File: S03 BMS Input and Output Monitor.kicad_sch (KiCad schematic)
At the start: 29 parts, among them Q4 DMP3007SCG-13, Q5 DMP3007SCG-13, U1 LTC1960

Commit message: Keep top copper out of power FET source-drain gaps; mask-layer logo
- Add F.Cu keepouts (no tracks/vias/pour) between source and drain pads
  in the TDSON, CSD17304Q3 and PowerDI3333 footprints, so a shorted FET
  can be reworked without bridging S-D through top copper.
- Add Diodes_PowerDI3333-8 (copy of the KiCad Package_SON footprint with
  the keepout) and point Q4/Q5/Q12-Q15 at it; drop the board-level
  Q5/Q7 keepouts.
- Move nine vias (Q17 GND, Q18 SW2) out of the S-D gaps.
- New dru rule "Power FET pad to pour": 0.3 mm zone-to-pad clearance on
  Q footprints, giving >=0.25 mm mask web around FET pads.
- Add EVOSONIC_DNA_LOGO_390X600_MASK footprint (F.Mask polygons) and
  use it for LOGO01.
- Schematic NOTE fields updated and pushed to the PCB; zones refilled.
- README notes on the keepouts and the 0.3 mm rule.

ERC 0 violations. DRC 0 unconnected, 0 parity; remaining items are
excluded layer-marker edge clearances, silk overlap and text thickness.

Co-Authored-By: Claude Opus 5.5 <noreply@anthropic.com>
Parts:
- Q4, Q5: footprint Package_SON:Diodes_PowerDI3333-8 -> EVO2513-0_5_0-import-fps:Diodes_PowerDI3333-8
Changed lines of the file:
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@@
 			)
 		)
-		(property "Footprint" "Package_SON:Diodes_PowerDI3333-8"
+		(property "Footprint" "EVO2513-0_5_0-import-fps:Diodes_PowerDI3333-8"
 			(at 260.35 83.82 0)
 			(hide yes)
@@
 			)
 		)
-		(property "Footprint" "Package_SON:Diodes_PowerDI3333-8"
+		(property "Footprint" "EVO2513-0_5_0-import-fps:Diodes_PowerDI3333-8"
 			(at 275.59 83.82 0)
 			(hide yes)

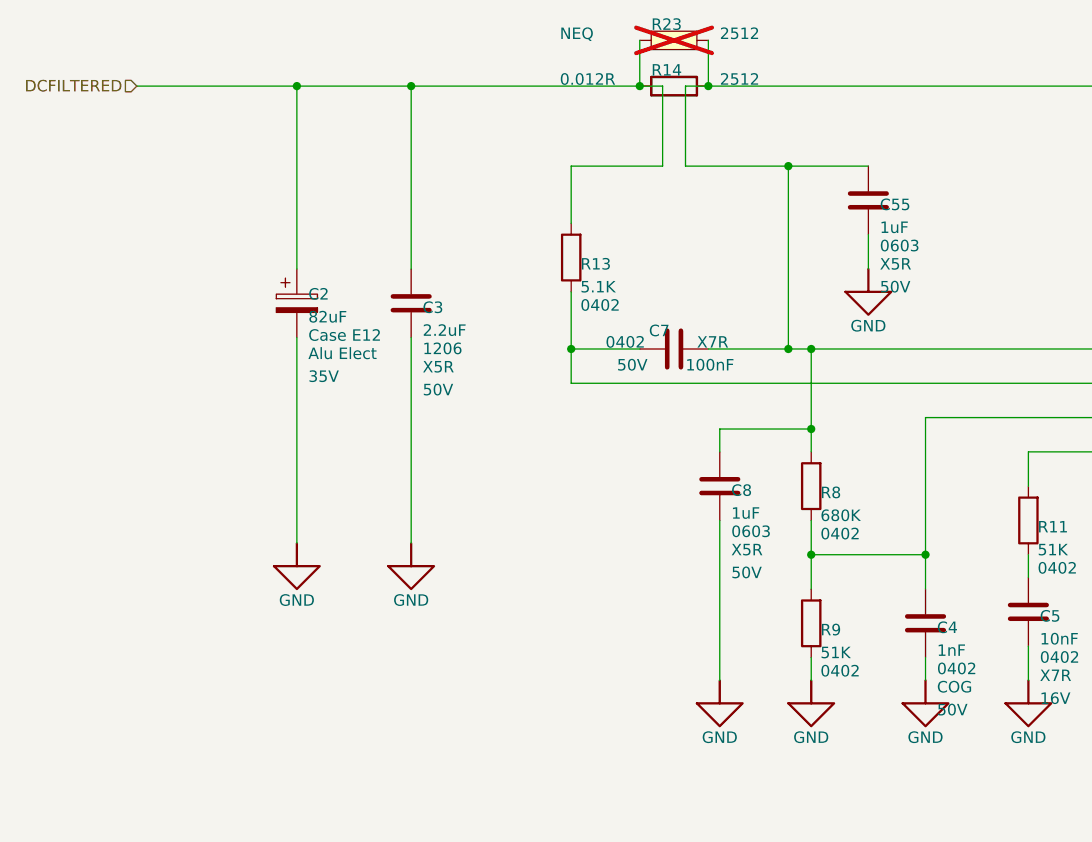
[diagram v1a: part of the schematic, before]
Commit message: Remove C55; charger layout; QC and S/N boxes
- C55 removed from the schematic and board.
- Charger-area placement and routing around U1 (C8, C7, R13, D3, DCSENSED).
- Filled QC and S/N marking boxes on the front silkscreen.

DRC: 23 violations (silk/text only), 0 unconnected, 0 parity.

Co-Authored-By: Claude Opus 5.5 <noreply@anthropic.com>
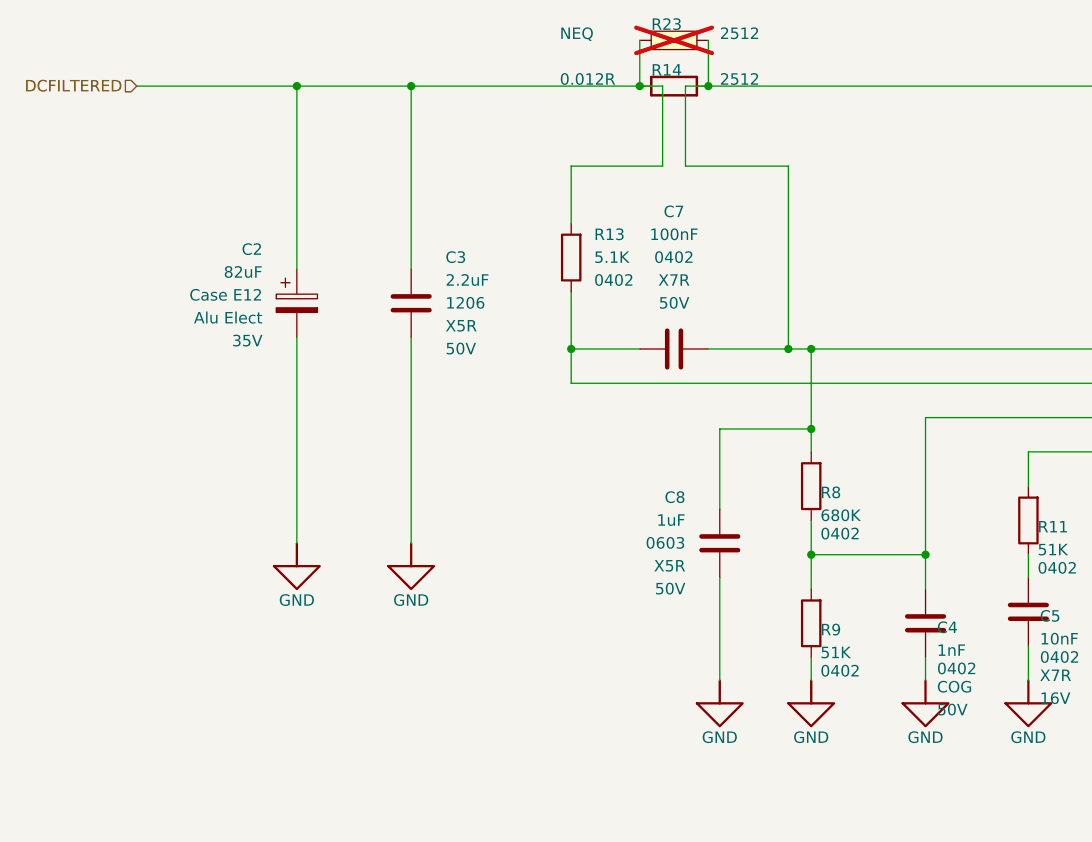
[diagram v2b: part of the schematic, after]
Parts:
- removed C55: 1uF, Capacitor_SMD:C_0603_1608Metric, symbol Device:C
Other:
- moved on the sheet: C8

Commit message: Fill manufacturer part numbers from the 0.5.0 build orders
Set MANUFACTURER and MANUFACTURER_PN on every fitted part, in the
schematic and on the board. Unchanged parts take the exact part numbers
ordered for the 0.5.0 backup build (DigiKey list and Mouser basket);
changed parts reuse an ordered part where value, package and rating
match; the rest keep the schematic's part or take a Yageo RC/CC part.

Co-Authored-By: Claude Opus 5.5 <noreply@anthropic.com>
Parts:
- C10, C7, R14: MANUFACTURER Yageo -> YAGEO
- C11, C12: MANUFACTURER Murata -> Murata Electronics
- C2: MANUFACTURER Panasonic -> Panasonic Industry
- C3: MANUFACTURER (none) -> YAGEO; MANUFACTURER_PN (none) -> CC1206KKX5R9BB225
- C4: MANUFACTURER (none) -> YAGEO; MANUFACTURER_PN (none) -> AC0402JRNPO9BN102
- C5: MANUFACTURER Murata -> Murata Electronics; MANUFACTURER_PN GRM155R71C103K -> GRM155R71C103KA01D
- C57: MANUFACTURER ? -> YAGEO; MANUFACTURER_PN ? -> CC0402JRNPO9BN101
- C6: MANUFACTURER (none) -> KEMET; MANUFACTURER_PN (none) -> C0402C182K4RACTU
- C8, C9: MANUFACTURER ? -> Samsung Electro-Mechanics; MANUFACTURER_PN ? -> CL10A105KB8NNNC
- R10: MANUFACTURER ? -> YAGEO; MANUFACTURER_PN ? -> RC0402FR-074K7L
- R11, R9: MANUFACTURER (none) -> YAGEO; MANUFACTURER_PN (none) -> RC0402FR-0751KL
- R12, R18: MANUFACTURER ? -> YAGEO; MANUFACTURER_PN ? -> RC0402FR-07100KL
- R13: MANUFACTURER ? -> YAGEO; MANUFACTURER_PN ? -> RC0402FR-075K1L
- R15: MANUFACTURER ? -> YAGEO; MANUFACTURER_PN ? -> RC0402FR-07100RL
- R16: MANUFACTURER Bourns -> Bourns Inc.
- R17: MANUFACTURER ? -> YAGEO; MANUFACTURER_PN ? -> RC0402FR-07619KL
- R8: MANUFACTURER (none) -> YAGEO; MANUFACTURER_PN (none) -> RC0402FR-07680KL
- U1: MANUFACTURER Analog Devices -> Analog Devices Inc.; MANUFACTURER_PN LTC1960CUHF -> LTC1960CUHF#PBF
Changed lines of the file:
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@@
 			)
 		)
-		(property "MANUFACTURER" "?"
+		(property "MANUFACTURER" "YAGEO"
 			(at 128.524 193.802 0)
 			(hide yes)
@@
 			)
 		)
-		(property "MANUFACTURER_PN" "?"
+		(property "MANUFACTURER_PN" "RC0402FR-07100KL"
 			(at 128.524 193.802 0)
 			(hide yes)
@@
 			)
 		)
-		(property "MANUFACTURER" "Analog Devices"
+		(property "MANUFACTURER" "Analog Devices Inc."
 			(at 193.802 130.81 0)
 			(hide yes)
@@
 			)
 		)
-		(property "MANUFACTURER_PN" "LTC1960CUHF"
+		(property "MANUFACTURER_PN" "LTC1960CUHF#PBF"
 			(at 193.802 130.81 0)
 			(hide yes)
@@
 			)
 		)
-		(property "MANUFACTURER" "?"
+		(property "MANUFACTURER" "Samsung Electro-Mechanics"
 			(at 220.98 137.922 0)
 			(hide yes)
@@
 			)
 		)
-		(property "MANUFACTURER_PN" "?"
+		(property "MANUFACTURER_PN" "CL10A105KB8NNNC"
 			(at 220.98 137.922 0)
 			(hide yes)
@@
 			)
 		)
-		(property "MANUFACTURER" "?"
+		(property "MANUFACTURER" "YAGEO"
 			(at 221.234 129.032 0)
 			(hide yes)
@@
 			)
 		)
-		(property "MANUFACTURER_PN" "?"
+		(property "MANUFACTURER_PN" "RC0402FR-07100RL"
 			(at 221.234 129.032 0)
 			(hide yes)
@@
 			)
 		)
-		(property "MANUFACTURER" ""
+		(property "MANUFACTURER" "YAGEO"
 			(at 85.09 103.632 0)
 			(hide yes)
@@
 			)
 		)
-		(property "MANUFACTURER_PN" ""
+		(property "MANUFACTURER_PN" "CC1206KKX5R9BB225"
 			(at 85.09 103.632 0)
 			(hide yes)
@@
 			)
 		)
-		(property "MANUFACTURER" "?"
+		(property "MANUFACTURER" "YAGEO"
 			(at 112.014 193.802 0)
 			(hide yes)
@@
 			)
 		)
-		(property "MANUFACTURER_PN" "?"
+		(property "MANUFACTURER_PN" "RC0402FR-074K7L"
 			(at 112.014 193.802 0)
 			(hide yes)
@@
 			)
 		)
-		(property "MANUFACTURER" "Yageo"
+		(property "MANUFACTURER" "YAGEO"
 			(at 111.252 111.76 90)
 			(hide yes)
@@
 			)
 		)
-		(property "MANUFACTURER" ""
+		(property "MANUFACTURER" "KEMET"
 			(at 162.052 138.43 0)
 			(hide yes)
@@
 			)
 		)
-		(property "MANUFACTURER_PN" ""
+		(property "MANUFACTURER_PN" "C0402C182K4RACTU"
 			(at 162.052 138.43 0)
 			(hide yes)
@@
 			)
 		)
-		(property "MANUFACTURER" "Panasonic"
+		(property "MANUFACTURER" "Panasonic Industry"
 			(at 72.39 103.632 0)
 			(hide yes)
@@
 			)
 		)
-		(property "MANUFACTURER" "Yageo"
+		(property "MANUFACTURER" "YAGEO"
 			(at 234.95 130.302 0)
 			(hide yes)
@@
 			)
 		)
-		(property "MANUFACTURER" "Analog Devices"
+		(property "MANUFACTURER" "Analog Devices Inc."
 			(at 164.592 224.79 0)
 			(hide yes)
@@
 			)
 		)
-		(property "MANUFACTURER_PN" "LTC1960CUHF"
+		(property "MANUFACTURER_PN" "LTC1960CUHF#PBF"
 			(at 164.592 224.79 0)
 			(hide yes)
@@
 			)
 		)
-		(property "MANUFACTURER" "Murata"
+		(property "MANUFACTURER" "Murata Electronics"
 			(at 256.54 181.102 0)
 			(hide yes)
@@
 			)
 		)
-		(property "MANUFACTURER" ""
+		(property "MANUFACTURER" "YAGEO"
 			(at 129.794 123.952 0)
 			(hide yes)
@@
 			)
 		)
-		(property "MANUFACTURER_PN" ""
+		(property "MANUFACTURER_PN" "RC0402FR-07680KL"
 			(at 129.794 123.952 0)
 			(hide yes)
@@
 			)
 		)
-		(property "MANUFACTURER" "?"
+		(property "MANUFACTURER" "YAGEO"
 			(at 254 220.472 0)
 			(hide yes)
@@
 			)
 		)
-		(property "MANUFACTURER_PN" "?"
+		(property "MANUFACTURER_PN" "CC0402JRNPO9BN101"
 			(at 254 220.472 0)
 			(hide yes)
@@
 			)
 		)
-		(property "MANUFACTURER" "?"
+		(property "MANUFACTURER" "Samsung Electro-Mechanics"
 			(at 119.38 130.302 0)
 			(hide yes)
@@
 			)
 		)
-		(property "MANUFACTURER_PN" "?"
+		(property "MANUFACTURER_PN" "CL10A105KB8NNNC"
 			(at 119.38 130.302 0)
 			(hide yes)
@@
 			)
 		)
-		(property "MANUFACTURER" ""
+		(property "MANUFACTURER" "YAGEO"
 			(at 153.924 127.762 0)
 			(hide yes)
@@
 			)
 		)
-		(property "MANUFACTURER_PN" ""
+		(property "MANUFACTURER_PN" "RC0402FR-0751KL"
 			(at 153.924 127.762 0)
 			(hide yes)
@@
 			)
 		)
-		(property "MANUFACTURER" "?"
+		(property "MANUFACTURER" "YAGEO"
 			(at 240.284 220.472 0)
 			(hide yes)
@@
 			)
 		)
-		(property "MANUFACTURER_PN" "?"
+		(property "MANUFACTURER_PN" "RC0402FR-07100KL"
 			(at 240.284 220.472 0)
 			(hide yes)
@@
 			)
 		)
-		(property "MANUFACTURER" ""
+		(property "MANUFACTURER" "YAGEO"
 			(at 139.192 139.7 0)
 			(hide yes)
@@
 			)
 		)
-		(property "MANUFACTURER_PN" ""
+		(property "MANUFACTURER_PN" "AC0402JRNPO9BN102"
 			(at 139.192 139.7 0)
 			(hide yes)
@@
 			)
 		)
-		(property "MANUFACTURER" ""
+		(property "MANUFACTURER" "YAGEO"
 			(at 129.794 139.192 0)
 			(hide yes)
@@
 			)
 		)
-		(property "MANUFACTURER_PN" ""
+		(property "MANUFACTURER_PN" "RC0402FR-0751KL"
 			(at 129.794 139.192 0)
 			(hide yes)
@@
 			)
 		)
-		(property "MANUFACTURER" "Yageo"
+		(property "MANUFACTURER" "YAGEO"
 			(at 111.252 80.01 90)
 			(hide yes)
@@
 			)
 		)
-		(property "MANUFACTURER" "Murata"
+		(property "MANUFACTURER" "Murata Electronics"
 			(at 153.67 137.922 0)
 			(hide yes)
@@
 			)
 		)
-		(property "MANUFACTURER_PN" "GRM155R71C103K"
+		(property "MANUFACTURER_PN" "GRM155R71C103KA01D"
 			(at 153.67 137.922 0)
 			(hide yes)
@@
 			)
 		)
-		(property "MANUFACTURER" "Murata"
+		(property "MANUFACTURER" "Murata Electronics"
 			(at 269.24 181.102 0)
 			(hide yes)
@@
 			)
 		)
-		(property "MANUFACTURER" "?"
+		(property "MANUFACTURER" "YAGEO"
 			(at 103.124 98.552 0)
 			(hide yes)
@@
 			)
 		)
-		(property "MANUFACTURER_PN" "?"
+		(property "MANUFACTURER_PN" "RC0402FR-075K1L"
 			(at 103.124 98.552 0)
 			(hide yes)
@@
 			)
 		)
-		(property "MANUFACTURER" "?"
+		(property "MANUFACTURER" "YAGEO"
 			(at 240.284 201.422 0)
 			(hide yes)
@@
 			)
 		)
-		(property "MANUFACTURER_PN" "?"
+		(property "MANUFACTURER_PN" "RC0402FR-07619KL"
 			(at 240.284 201.422 0)
 			(hide yes)
@@
 			)
 		)
-		(property "MANUFACTURER" "Bourns"
+		(property "MANUFACTURER" "Bourns Inc."
 			(at 207.772 168.91 90)
 			(hide yes)

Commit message: Match D1 and R14 to the parts held, standardise resistors on Yageo
D1 is the Diotec 1.0SMBJ26CA and R14 the Yageo PA2512FKE7W0R012E, as
received. R31 and R111-R114 move to Yageo so every resistor except the
current-sense shunts comes from one manufacturer.

Co-Authored-By: Claude Opus 5.5 <noreply@anthropic.com>
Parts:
- R14: MANUFACTURER_PN PA2512FKF7W0R012E -> PA2512FKE7W0R012E
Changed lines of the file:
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@@
 			)
 		)
-		(property "MANUFACTURER_PN" "PA2512FKF7W0R012E"
+		(property "MANUFACTURER_PN" "PA2512FKE7W0R012E"
 			(at 111.252 80.01 90)
 			(hide yes)

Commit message: Move capacitors to currently available part numbers
C32 to Murata GRM219R61C226ME15L (GRM21BR61C226ME44L is no longer
generally available), C39 to Yageo CC0805KPX7R9BB102, the 1 uF 0603
caps to Murata GRT188R61H105KE13D, and the 10 uF 1210 caps to Taiyo
Yuden UMK325AB7106KMHP.

Co-Authored-By: Claude Opus 5.5 <noreply@anthropic.com>
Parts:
- C11, C12: MANUFACTURER Murata Electronics -> Taiyo Yuden; MANUFACTURER_PN GRM32ER71H106KA12L -> UMK325AB7106KMHP
- C8, C9: MANUFACTURER Samsung Electro-Mechanics -> Murata Electronics; MANUFACTURER_PN CL10A105KB8NNNC -> GRT188R61H105KE13D
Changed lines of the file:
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@@
 			)
 		)
-		(property "MANUFACTURER" "Samsung Electro-Mechanics"
+		(property "MANUFACTURER" "Murata Electronics"
 			(at 220.98 137.922 0)
 			(hide yes)
@@
 			)
 		)
-		(property "MANUFACTURER_PN" "CL10A105KB8NNNC"
+		(property "MANUFACTURER_PN" "GRT188R61H105KE13D"
 			(at 220.98 137.922 0)
 			(hide yes)
@@
 			)
 		)
-		(property "MANUFACTURER" "Murata Electronics"
+		(property "MANUFACTURER" "Taiyo Yuden"
 			(at 256.54 181.102 0)
 			(hide yes)
@@
 			)
 		)
-		(property "MANUFACTURER_PN" "GRM32ER71H106KA12L"
+		(property "MANUFACTURER_PN" "UMK325AB7106KMHP"
 			(at 256.54 181.102 0)
 			(hide yes)
@@
 			)
 		)
-		(property "MANUFACTURER" "Samsung Electro-Mechanics"
+		(property "MANUFACTURER" "Murata Electronics"
 			(at 119.38 130.302 0)
 			(hide yes)
@@
 			)
 		)
-		(property "MANUFACTURER_PN" "CL10A105KB8NNNC"
+		(property "MANUFACTURER_PN" "GRT188R61H105KE13D"
 			(at 119.38 130.302 0)
 			(hide yes)
@@
 			)
 		)
-		(property "MANUFACTURER" "Murata Electronics"
+		(property "MANUFACTURER" "Taiyo Yuden"
 			(at 269.24 181.102 0)
 			(hide yes)
@@
 			)
 		)
-		(property "MANUFACTURER_PN" "GRM32ER71H106KA12L"
+		(property "MANUFACTURER_PN" "UMK325AB7106KMHP"
 			(at 269.24 181.102 0)
 			(hide yes)
